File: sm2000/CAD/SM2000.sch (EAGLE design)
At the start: 398 parts, among them CN1 HDR100-3, CN2 ST-3509, CN3 HDR100-3, CN4 JS-MU3-002, CN5 DS-0518, CN6 ST-3509, CN7 ST-3509, J1 JMP-2PIN, J10 JMPR-2X2, J11 JMPR-2X2, J12 JMPR-2X2, J13 JMPR-2X2, J14 JMPR-2X2, J2 HDR100-5, J3 JMP-2PIN, J4 CONN-BOOM-XH-2A, J5 JMP-2PIN, J6 JMPR-2X2, J7 JMPR-2X2, J8 JMPR-2X2, J9 JMPR-2X2, P1 TPAD50, P10 TPAD50, P12 TPAD50, P13 TPAD50, P2 TPAD50, P3 TPAD50, P4 TPAD50, P5 TPAD50, P6 TPAD50, P7 TPAD50, P8 TPAD50, P9 TPAD50, Q1 MMBT3904, Q10 MMBT3904, Q11 BRF92, Q12 BFQ19, Q13 RD01MUS2, Q14 MMBT3904, Q15 MMBT3904, Q16 MMBT3904, Q17 MMBT3906, Q2 STR2P3LLH6, Q3 MMBT3904, Q4 STR2P3LLH6, Q5 MMBT3904, Q6 MMBT3904, Q7 MMBT3904, Q8 MMBT3904, Q9 MMBT3904, SW1 TS-02B, SW2 SW-LC2259, SW3 TS-026, SW4 TS-026, SW5 SW-LC2259EENP, U1 STM32F405VGT6, U10 LM386M-1, U11 ADE-1, U12 PGA-103+, U13 LMV341, U14 SI5351A, U15 SI570, U16 SA612A, U2 STMPS2141, U3 EMIF02-USB03F2, U4 DNL, U5 L78MXX, U6 L78MXX, U7 LMV341, U8 AP7215Y-33, U9 TPS54329E, X1 BU-SMA-H

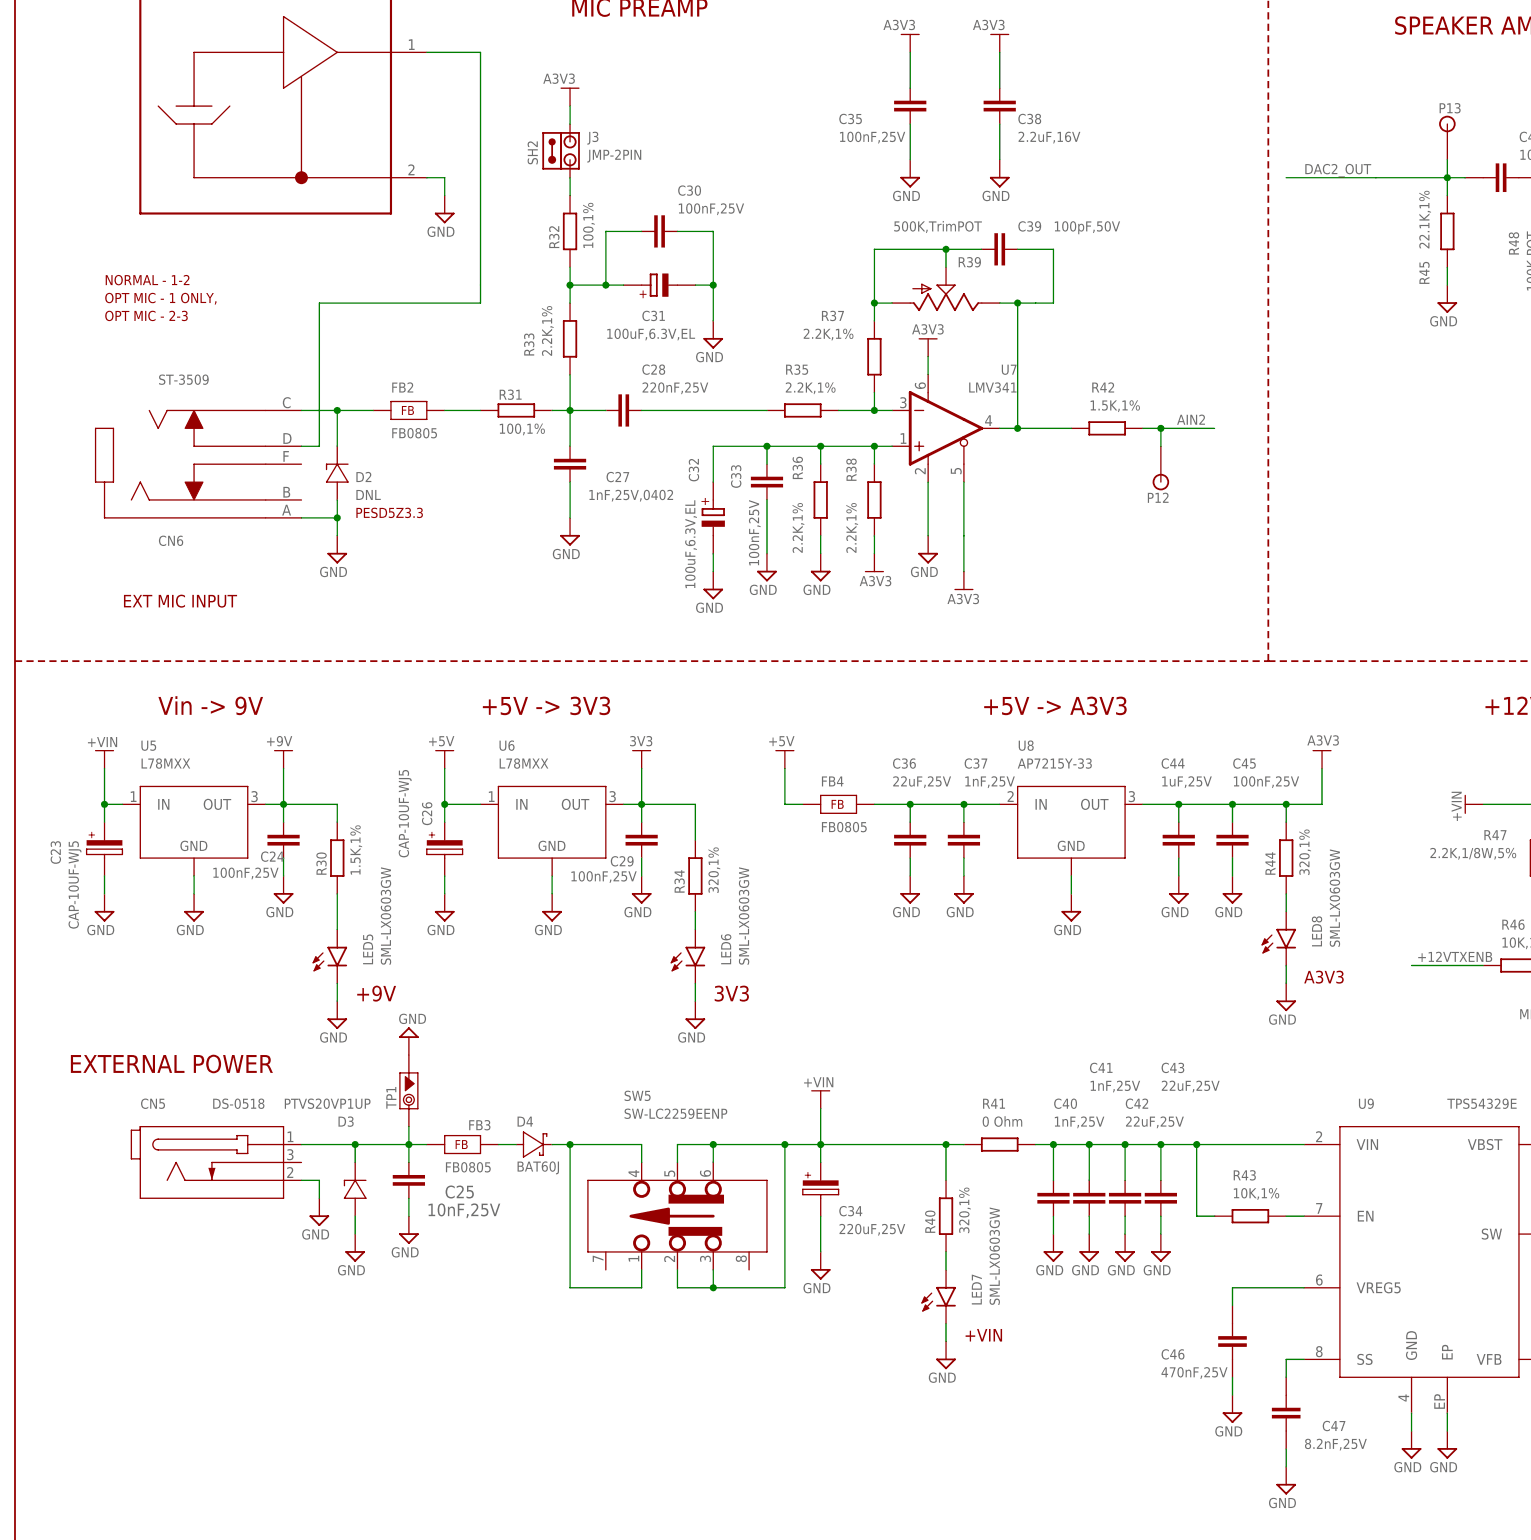
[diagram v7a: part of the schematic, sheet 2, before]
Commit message: Added scope test points per signal list, Made edits per latest email(Jan 19,2016 03:31pm. Created scope test point symbol footprint and component. Edited rowetel.lbr to make resistor & capacitor components consistent. Movinf power supply related components onto PCB to start layout. RGB
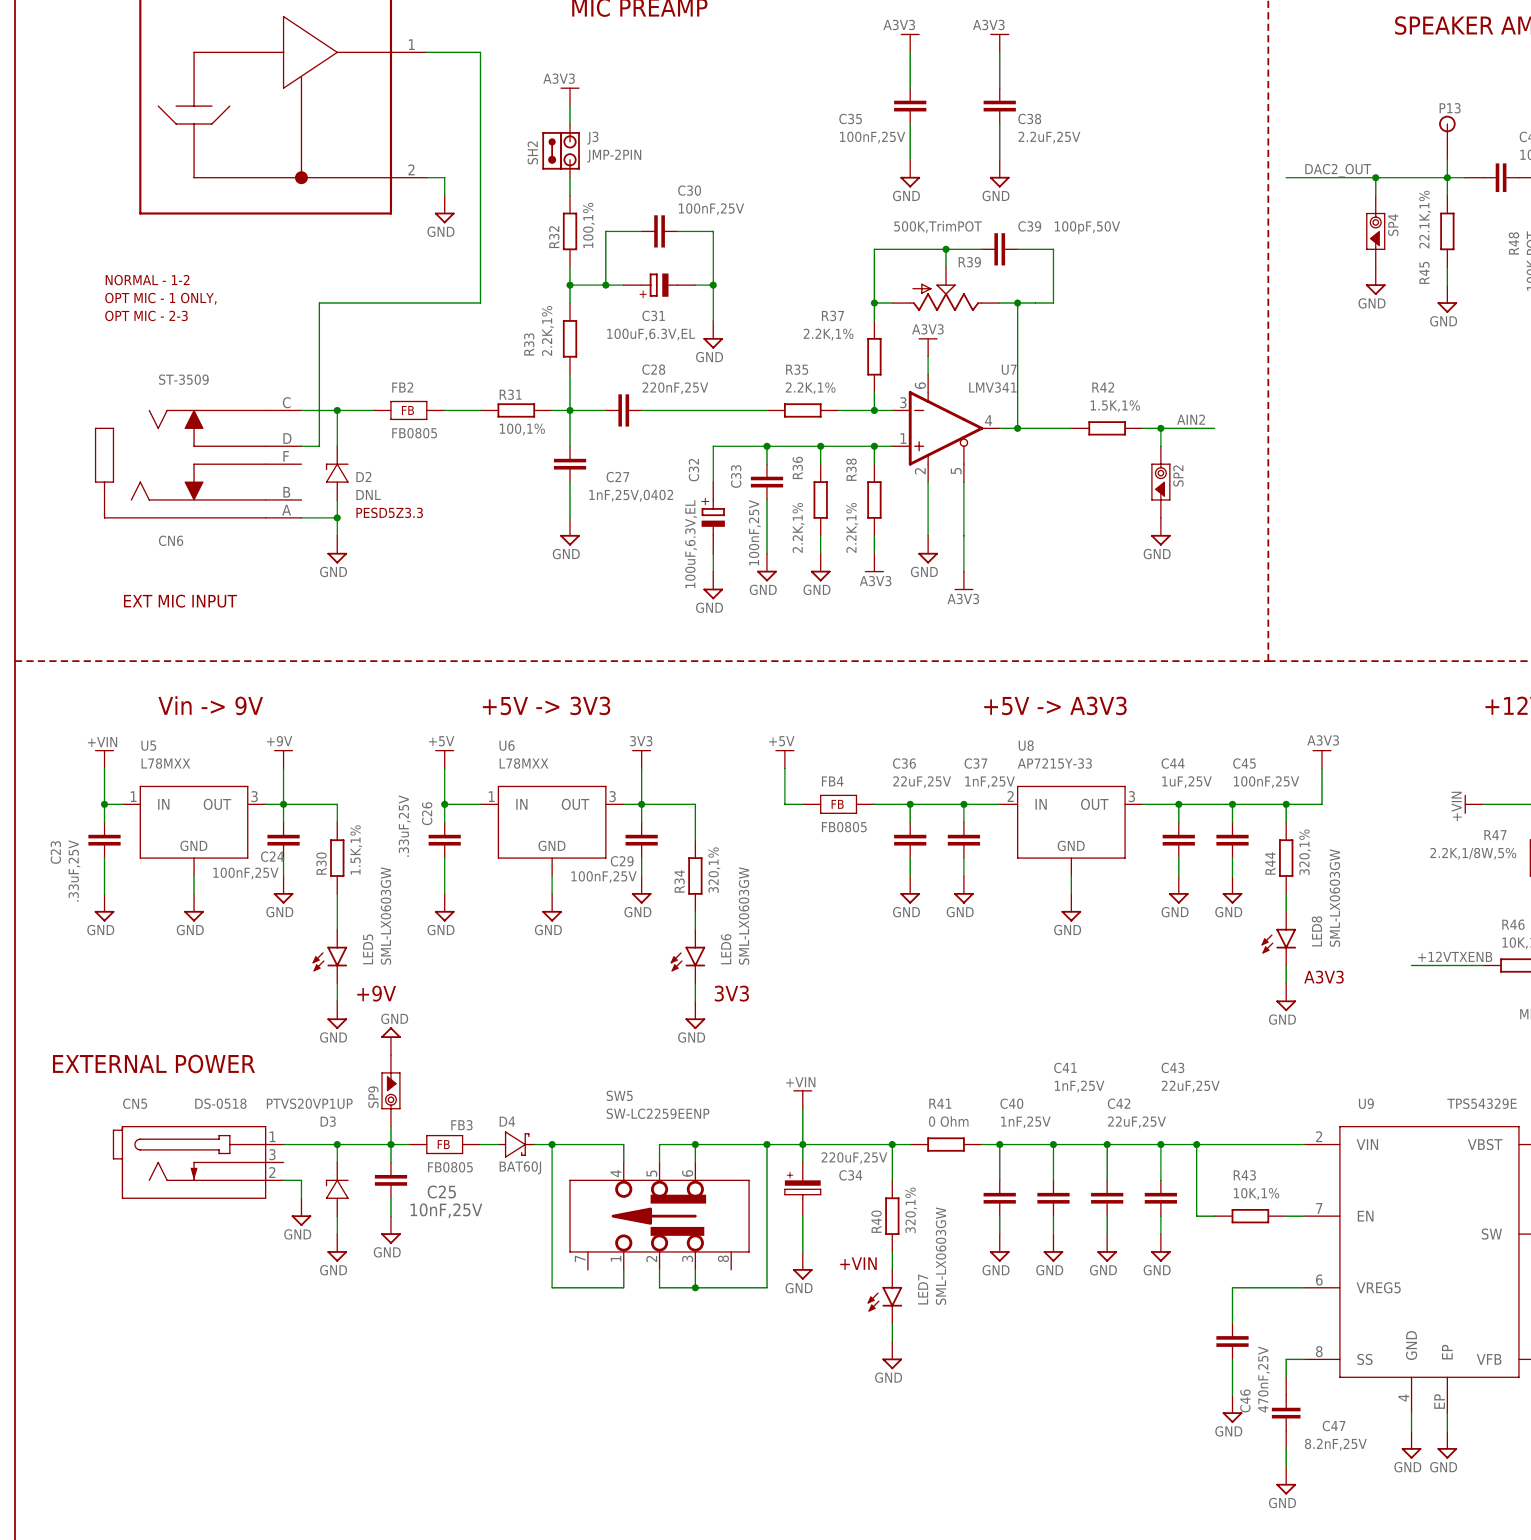
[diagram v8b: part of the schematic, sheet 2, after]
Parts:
- removed P12: TPAD50, _Coherix:TPAD50
- removed TP1: SCOPE_PAD, _RoweTel:SCOPE_PAD
- added SP1, SP2, SP3, SP4, SP5, SP6, SP7, SP8, SP9: SCOPE_PAD, _RoweTel:SCOPE_PAD
- C23, C26: value CAP-10UF-WJ5 -> .33uF,25V; device _RoweTel:CAP-10UF-WJ5 -> _RoweTel:CAP-0603
- C24, C25, C29, C37, C40, C41, C44, C45: device _RoweTel:CAP-0805 -> _RoweTel:CAP-0603
- C27, C28, C30, C33, C35, C39: device _RoweTel:CAP-0805 -> _RoweTel:CAP-0402
- C38: value 2.2uF,16V -> 2.2uF,25V; device _RoweTel:CAP-0805 -> _RoweTel:CAP-0402
- C42, C43: device _RoweTel:CAP-1210 -> _RoweTel:CAP-0603
- C46: device AA-ipc-7351-capacitor:CAPACITOR_0603 -> _RoweTel:CAP-0603
- J2: value HDR100-5 -> HDR100-7; device _RoweTel:HDR100-5 -> _RoweTel:HDR100-7
- Q11: value BRF92 -> BFR92
- Q14, Q15: device transistor:-NPN-SOT23-EBC -> _RoweTel:MMBT3904
- Q17: device transistor-pnp:2N2905 -> _RoweTel:MMBT3906
- R1, R10, R11, R12, R13, R14, R16, R17, R18, R2, R21, R22, R24, R25, R26, R27, R28, R29, R3, R30, R34, R4, R40, R44, R46, R47, R5, R50, R54, R55, R56, R57, R6, R7, R8, R9: device _RoweTel:RES-0805 -> _RoweTel:RES-0402
- R19, R20, R23, R33, R35, R36, R38, R42, R43, R51, R52: device AA-ipc-7351-resistor:RESISTOR_0402 -> _RoweTel:RES-0402
- R31, R32, R41, R45, R53: device AA-ipc-7351-resistor:RESISTOR_0603 -> _RoweTel:RES-0402
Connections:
- removed net AIN_PWR: C97.2, D10.K
- removed net N$110: Q17.C, R118.2
- removed net TX2NDLO: C121.2, C128.1
- new net AIN3: C97.2, D10.K, U1A.PA3
- net +12VRXENB: now also J2.7
- net +12VTXENB: now also J2.6
- net 1ST_LO: now also SP6.1
- net AIN1: now also Q17.C, R118.2, SP1.1
- net AIN2: now also SP2.1; no longer P12.1
- net DAC2_OUT: now also SP4.1
- net GND: now also SP1.2, SP2.2, SP3.2, SP4.2, SP5.2, SP6.2, SP7.2, SP8.2, SP9.2; no longer TP1.2
- net N$77: now also SP9.1; no longer TP1.1
- net RX-2ND-LO: now also C128.1, SP8.1
- net TX-2ND-LO: now also C121.2, SP7.1
- net TX_DAC: now also SP3.1, U1A.PA4; no longer U1A.PA7
- net VGG: now also SP5.1
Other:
- note removed: "ADC3"
- note removed: "Vgg from uC DAC"
- moved on the sheet: C10, C118, C13, C25, C34, C40, C41, C42, CN5, D3, D4, FB3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
